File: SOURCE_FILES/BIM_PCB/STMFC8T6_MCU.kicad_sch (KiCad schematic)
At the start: 41 parts, among them J2 programming, J8 Conn_01x06, Q2 BSS123, Q3 BSS123, SW1 reset, U2 STM32F103C8Tx, Y1 8MHz, Y2 32.678KHz

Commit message: updates on schematic and complete layout
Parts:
- removed J2: programming, symbol Connector_Generic:Conn_01x05
- added H1, H2, H3, H4: MountingHole, MountingHole:MountingHole_2.7mm, symbol Mechanical:MountingHole
- added J2: Conn_02x03_Odd_Even, Connector_Molex:Molex_Mini-Fit_Jr_5569-06A2_2x03_P4.20mm_Horizontal, symbol Connector_Generic:Conn_02x03_Odd_Even
- J4: renamed from J?; footprint (none) -> Connector_Molex:Molex_Mini-Fit_Jr_5569-10A2_2x05_P4.20mm_Horizontal; MPN (none) -> HC-5557-2*5AW
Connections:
- net GND: now also J2.5 (Pin_5), J2.6 (Pin_6)
- net RESET: now also J2.4 (Pin_4)
- net SW0: now also J2.2 (Pin_2)
- net swdclk: now also J2.3 (Pin_3)
- net swdio: now also J2.1 (Pin_1)
- net RS485_~{RE}: now reaches U2.2 (PC13)
- net RS485_EN renamed RS485_DE
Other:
- moved on the sheet: C20, Q3, R7

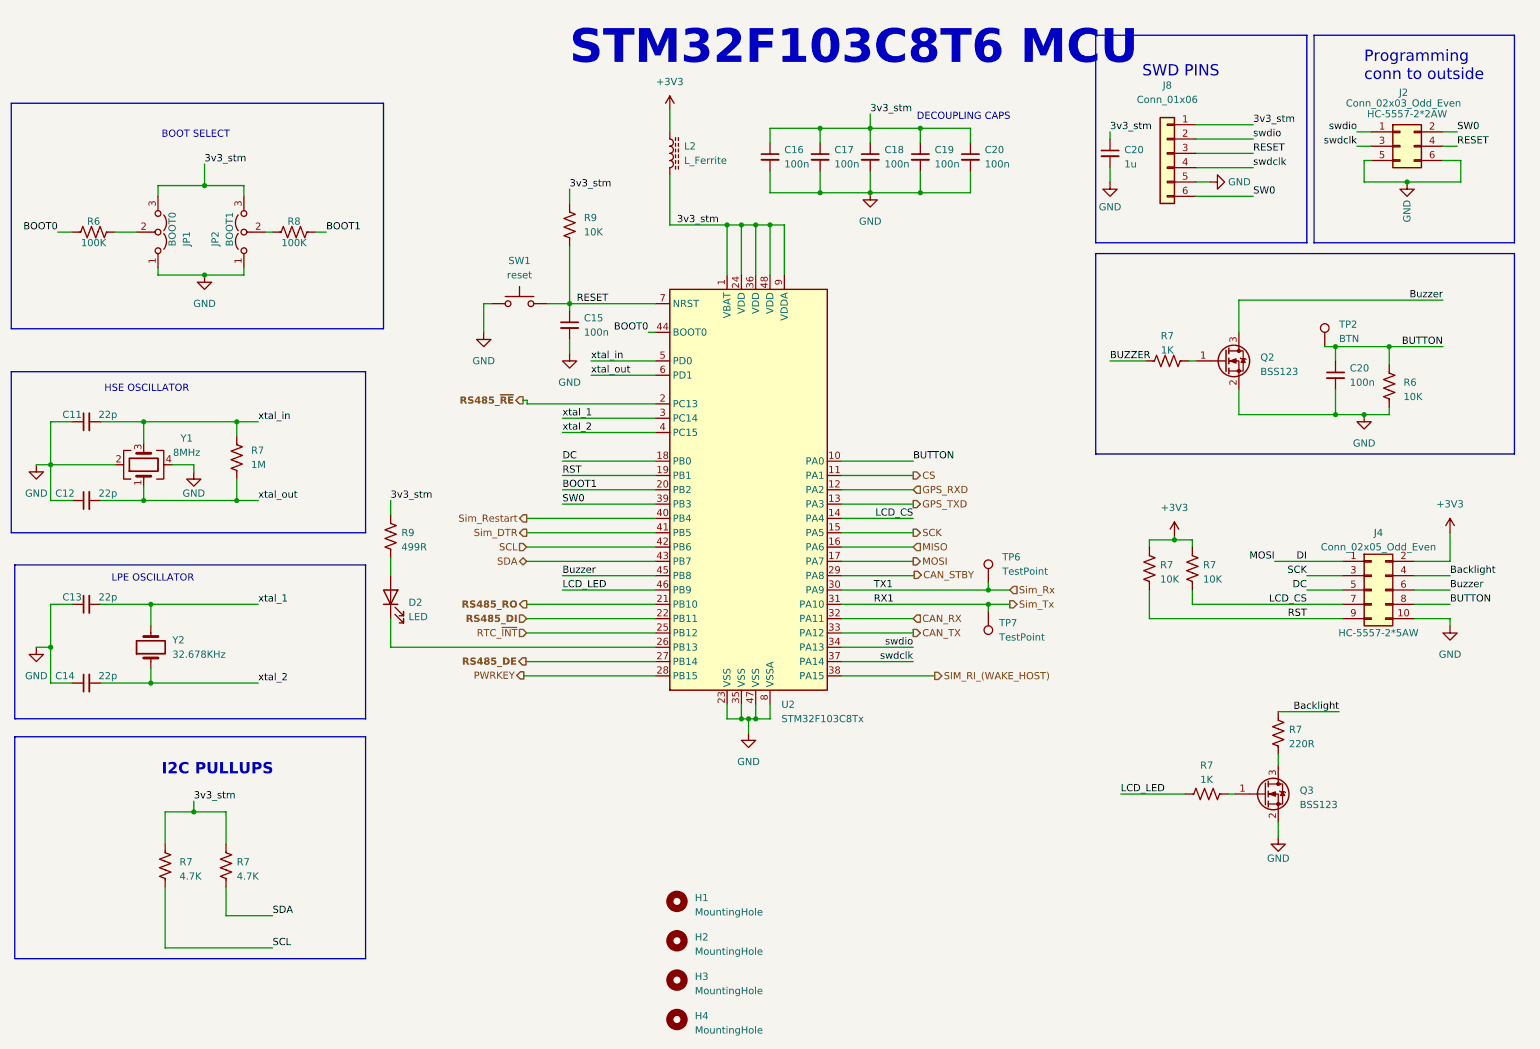
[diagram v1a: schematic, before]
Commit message: completed design PCN and Images
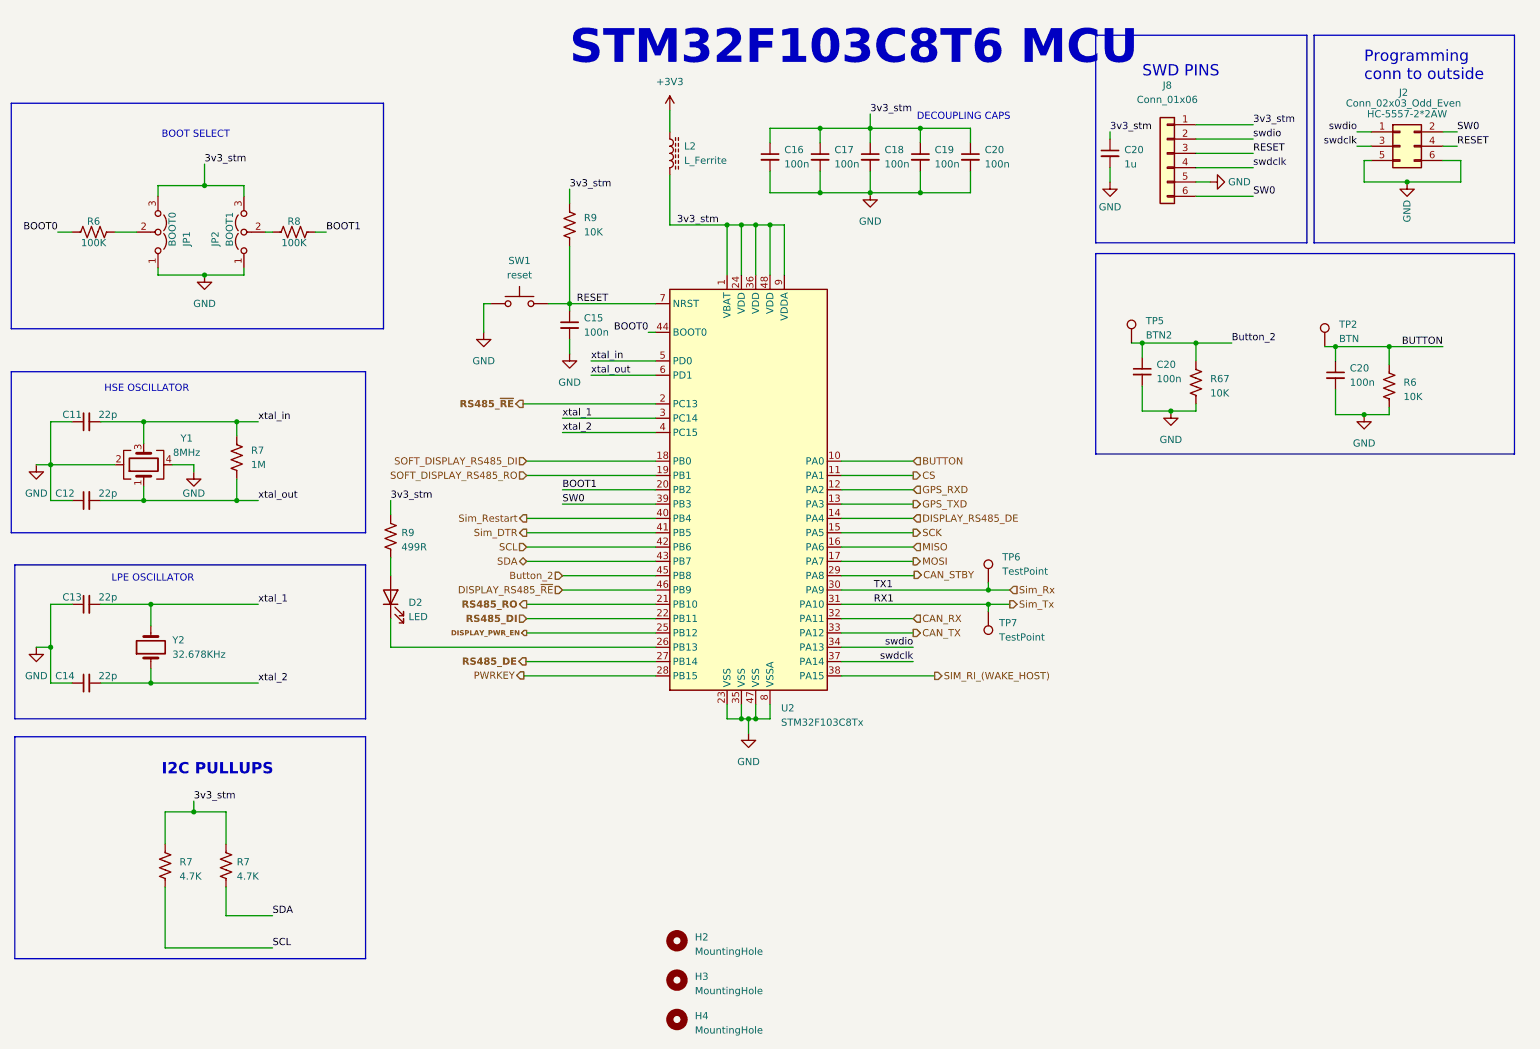
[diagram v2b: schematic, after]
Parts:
- removed H1: MountingHole, MountingHole:MountingHole_2.7mm, symbol Mechanical:MountingHole
- removed J4: Conn_02x05_Odd_Even, Connector_Molex:Molex_Mini-Fit_Jr_5569-10A2_2x05_P4.20mm_Horizontal, symbol Connector_Generic:Conn_02x05_Odd_Even
- removed Q2, Q3: BSS123, Package_TO_SOT_SMD:SOT-23, symbol Transistor_FET:BSS123
- removed R7 (x2): 10K, Resistor_SMD:R_0402_1005Metric, symbol Device:R_US
- removed R7 (x2): 1K, Resistor_SMD:R_0402_1005Metric, symbol Device:R_US
- removed R7: 220R, Resistor_SMD:R_0402_1005Metric, symbol Device:R_US
- added C20: 100n, Capacitor_SMD:C_0402_1005Metric, symbol Device:C_Small
- added R67: 10K, Resistor_SMD:R_0402_1005Metric, symbol Device:R_US
- added TP5: BTN2, brilliant-kicad-library:TestPoint_Pad_D0.9mm, symbol Connector:TestPoint
- J2: footprint Connector_Molex:Molex_Mini-Fit_Jr_5569-06A2_2x03_P4.20mm_Horizontal -> Connector_Molex:Molex_Nano-Fit_105314-xx06_2x03_P2.50mm_Horizontal
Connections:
- net GND: now also C20.2, R67.2
- net Buzzer renamed Button_2
- net Button_2: now also C20.1, R67.1, TP5.1
- net DC renamed SOFT_DISPLAY_RS485_DI
- net LCD_CS renamed DISPLAY_RS485_DE
- net LCD_LED renamed DISPLAY_RS485_~{RE}
- net RST renamed SOFT_DISPLAY_RS485_RO
- net RTC_~{INT} renamed DISPLAY_PWR_EN

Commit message: complete BIM Board
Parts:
- added TP7: PA4, brilliant-kicad-library:TestPoint_Pad_D0.9mm, symbol Connector:TestPoint
- added TP8: PB9, brilliant-kicad-library:TestPoint_Pad_D0.9mm, symbol Connector:TestPoint
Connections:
- net SEL: now reaches D2.1 (K), U2.26 (PB13)
- net DISPLAY_RS485_DE: no longer names the net of U2.14 (PA4)
- net DISPLAY_RS485_DE: now also TP7.1
- net DISPLAY_RS485_~{RE}: no longer names the net of U2.46 (PB9)
- net DISPLAY_RS485_~{RE}: now also TP8.1
- net SOFT_DISPLAY_RS485_DI renamed MUX_SEL_A
- net SOFT_DISPLAY_RS485_RO renamed MUX_SEL_B
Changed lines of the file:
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@@
   (junction (at 151.765 51.435) (diameter 0) (color 0 0 0 0)
   )
+  (junction (at 93.98 126.365) (diameter 0) (color 0 0 0 0)
+  )
   (junction (at 261.62 73.025) (diameter 0) (color 0 0 0 0)
   )
@@
     (stroke (width 0) (type default))
   )
+  (wire (pts (xy 84.455 126.365) (xy 84.455 121.285))
+    (stroke (width 0) (type default))
+  )
   (wire (pts (xy 151.765 34.29) (xy 151.765 36.83))
     (stroke (width 0) (type default))
@@
     (stroke (width 0) (type default))
   )
-  (wire (pts (xy 84.455 121.285) (xy 84.455 126.365))
-    (stroke (width 0) (type default))
-  )
   (polyline (pts (xy 80.01 106.045) (xy 17.145 106.045))
     (stroke (width 0) (type default))
@@
     (stroke (width 0) (type default))
   )
+  (wire (pts (xy 93.98 126.365) (xy 84.455 126.365))
+    (stroke (width 0) (type default))
+  )
   (polyline (pts (xy 80.01 111.76) (xy 80.01 139.065))
     (stroke (width 0) (type default))
@@
     (stroke (width 0) (type default))
   )
+  (wire (pts (xy 90.17 128.27) (xy 93.98 128.27))
+    (stroke (width 0) (type default))
+  )
   (wire (pts (xy 151.765 136.525) (xy 151.765 139.065))
     (stroke (width 0) (type default))
@@
     (stroke (width 0) (type default))
   )
-  (wire (pts (xy 131.445 126.365) (xy 84.455 126.365))
+  (wire (pts (xy 93.98 126.365) (xy 131.445 126.365))
     (stroke (width 0) (type default))
   )
@@
   )
   (polyline (pts (xy 17.145 29.845) (xy 83.185 29.845))
+    (stroke (width 0) (type default))
+  )
+  (wire (pts (xy 93.98 128.27) (xy 93.98 126.365))
     (stroke (width 0) (type default))
   )
@@
     (effects (font (size 1.27 1.27)) (justify left bottom))
   )
+  (hierarchical_label "SEL" (shape output) (at 90.17 128.27 180) (fields_autoplaced)
+    (effects (font (size 1.27 1.27)) (justify right))
+  )
   (hierarchical_label "CAN_STBY" (shape output) (at 177.336 113.5232 0) (fields_autoplaced)
     (effects (font (size 1.27 1.27)) (justify left))
@@
     (effects (font (size 1.27 1.27) bold) (justify right))
   )
-  (hierarchical_label "SOFT_DISPLAY_RS485_DI" (shape input) (at 108.585 93.345 180) (fields_autoplaced)
-    (effects (font (size 1.27 1.27)) (justify right))
-  )
-  (hierarchical_label "DISPLAY_RS485_~{RE}" (shape input) (at 114.935 116.205 180) (fields_autoplaced)
+  (hierarchical_label "MUX_SEL_A" (shape output) (at 108.585 93.345 180) (fields_autoplaced)
     (effects (font (size 1.27 1.27)) (justify right))
   )
@@
     (effects (font (size 1.27 1.27)) (justify left))
   )
-  (hierarchical_label "SOFT_DISPLAY_RS485_RO" (shape input) (at 108.585 95.885 180) (fields_autoplaced)
+  (hierarchical_label "MUX_SEL_B" (shape output) (at 108.585 95.885 180) (fields_autoplaced)
     (effects (font (size 1.27 1.27)) (justify right))
   )
@@
   (hierarchical_label "Sim_DTR" (shape output) (at 108.585 106.045 180) (fields_autoplaced)
     (effects (font (size 1.27 1.27)) (justify right))
-  )
-  (hierarchical_label "DISPLAY_RS485_DE" (shape input) (at 177.165 103.505 0) (fields_autoplaced)
-    (effects (font (size 1.27 1.27)) (justify left))
   )
   (hierarchical_label "Sim_Tx" (shape output) (at 194.31 118.745 0) (fields_autoplaced)
@@
     )
   )
+  (symbol (lib_id "Connector:TestPoint") (at 114.935 116.205 90) (unit 1)
+    (in_bom yes) (on_board yes) (dnp no)
+    (property "Reference" "TP8" (at 103.505 116.205 90)
+      (effects (font (size 1.27 1.27)))
+    )
+    (property "Value" "PB9" (at 108.585 116.205 90)
+      (effects (font (size 1.27 1.27)))
+    )
+    (property "Footprint" "brilliant-kicad-library:TestPoint_Pad_D0.9mm" (at 114.935 111.125 0)
+      (effects (font (size 1.27 1.27)) hide)
+    )
+    (property "Datasheet" "~" (at 114.935 111.125 0)
+      (effects (font (size 1.27 1.27)) hide)
+    )
+    (pin "1")
+    (instances
+      (project "BIM_PCB"
+        (path "/b79ebed7-e146-448b-8dab-0aefb3e182ca/f23c600c-7725-4edd-91d3-0267a41a1c43"
+          (reference "TP8") (unit 1)
+        )
+      )
+    )
+  )
   (symbol (lib_id "power:GND") (at 169.545 45.72 0) (unit 1)
     (in_bom yes) (on_board yes) (dnp no) (fields_autoplaced)
@@
         )
       )
+    )
+  )
+  (symbol (lib_id "Connector:TestPoint") (at 177.165 103.505 270) (unit 1)
+    (in_bom yes) (on_board yes) (dnp no)
+    (property "Reference" "TP7" (at 188.595 103.505 90)
+      (effects (font (size 1.27 1.27)))
+    )
+    (property "Value" "PA4" (at 183.515 103.505 90)
+      (effects (font (size 1.27 1.27)))
+    )
+    (property "Footprint" "brilliant-kicad-library:TestPoint_Pad_D0.9mm" (at 177.165 108.585 0)
+      (effects (font (size 1.27 1.27)) hide)
+    )
+    (property "Datasheet" "~" (at 177.165 108.585 0)
+      (effects (font (size 1.27 1.27)) hide)
+    )
+    (pin "1")
+    (instances
+      (project "BIM_PCB"
+        (path "/b79ebed7-e146-448b-8dab-0aefb3e182ca/f23c600c-7725-4edd-91d3-0267a41a1c43"
+          (reference "TP7") (unit 1)
+        )
+      )
